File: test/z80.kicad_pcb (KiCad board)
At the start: 2 copper layers, 71.1 x 43.2 mm, 53 parts, among them U1 74AHC1G14

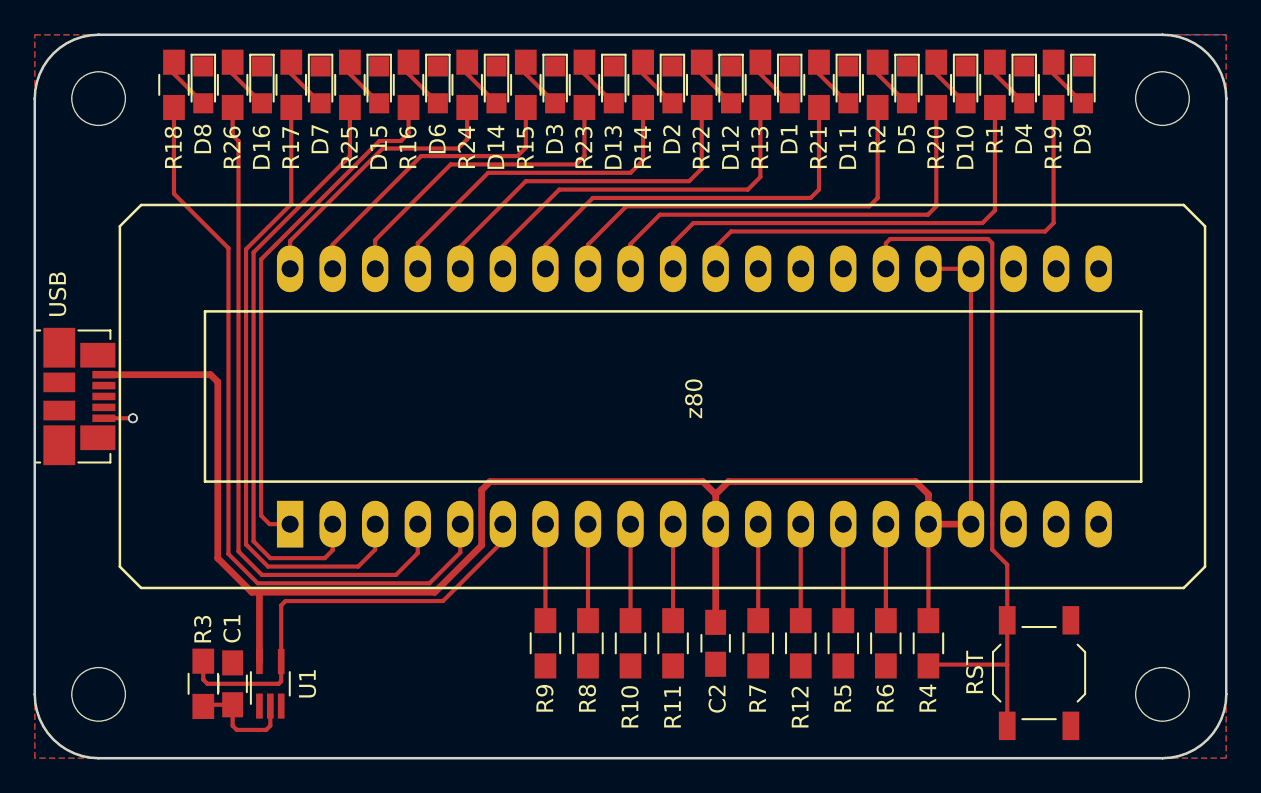
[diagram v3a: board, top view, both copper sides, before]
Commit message: Renumber data pulldowns and address LEDs to match bits
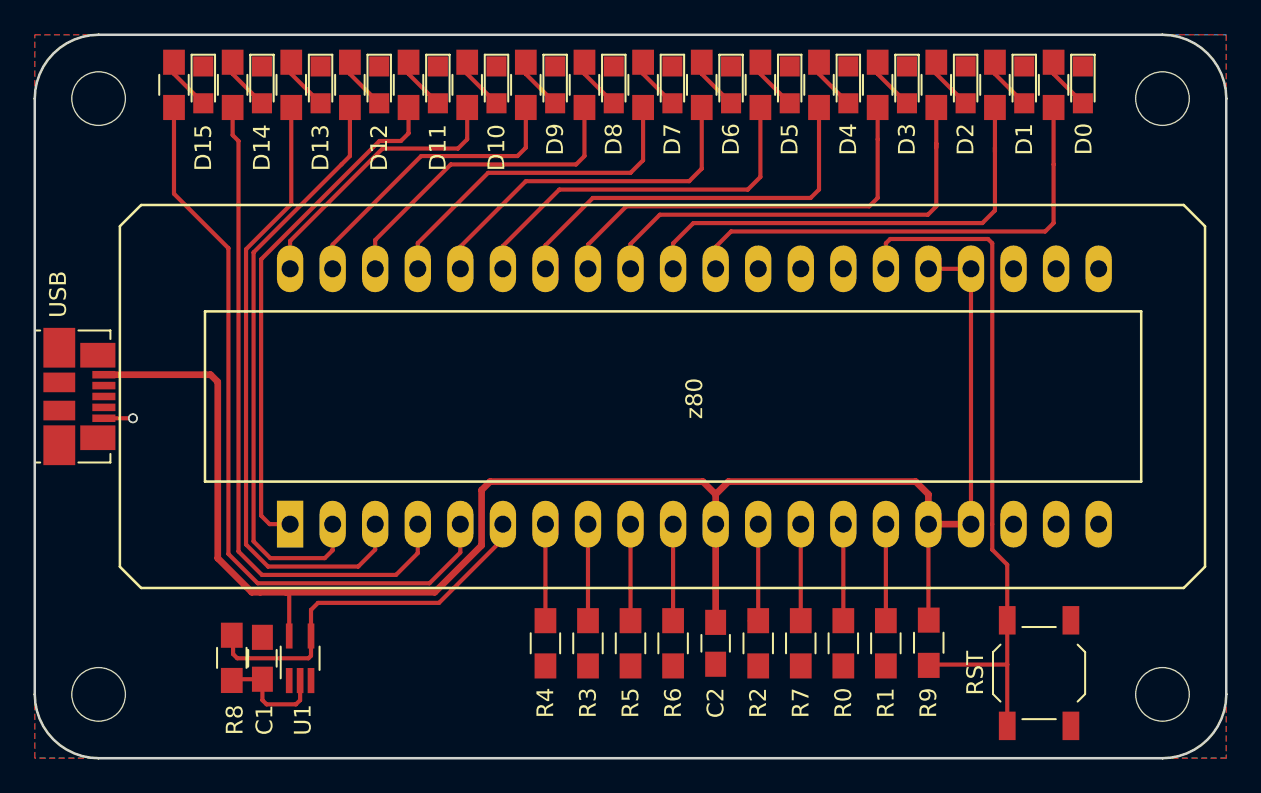
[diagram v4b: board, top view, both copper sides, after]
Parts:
- removed D16: LED, LEDs:LED_0805
- removed R12: 10k, Resistors_SMD:R_0805_HandSoldering
- added D0: LED, LEDs:LED_0805, F.Cu at (217.5, 83.0)
- added R0: 10k, Resistors_SMD:R_0805_HandSoldering, F.Cu at (203.2, 116.3)
- R1, R2: value 470R -> 10k
- R10, R11: value 10k -> 470R
- R3: value 68k -> 10k
- R8: value 10k -> 68k
- moved R10 39.8 mm to (212.2, 83.0), turned to 270 degrees
- moved R11 35.5 mm to (205.2, 83.0), turned to 270 degrees
- moved R2 34.1 mm to (198.1, 116.3), turned to 90 degrees
- moved R1 34.0 mm to (205.7, 116.3), turned to 90 degrees
- moved D9 31.5 mm to (186.0, 83.0)
- moved D10 28.0 mm to (182.5, 83.0)
- moved D11 24.5 mm to (179.0, 83.0)
- moved D8 24.5 mm to (189.5, 83.0)
- moved R3 23.1 mm to (188.0, 116.3), turned to 90 degrees
- moved R9 22.9 mm to (208.3, 116.3), turned to 270 degrees
- moved R4 22.9 mm to (185.4, 116.3), turned to 90 degrees
- moved R8 21.3 mm to (166.7, 117.2), turned to 270 degrees
- moved D12 21.0 mm to (175.5, 83.0)
- moved D3 21.0 mm to (207.0, 83.0)
- moved D7 21.0 mm to (193.0, 83.0)
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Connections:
- R1 pad 1: Net-(D4-Pad2) -> GND
- R10 pad 1: GND -> Net-(D1-Pad2)
- R11 pad 1: GND -> Net-(D3-Pad2)
- R13 pad 1: Net-(D1-Pad2) -> Net-(D5-Pad2)
- R14 pad 1: Net-(D2-Pad2) -> Net-(D7-Pad2)
- R15 pad 1: Net-(D3-Pad2) -> Net-(D9-Pad2)
- R16 pad 1: Net-(D6-Pad2) -> Net-(D11-Pad2)
- R17 pad 1: Net-(D7-Pad2) -> Net-(D13-Pad2)
- R18 pad 1: Net-(D8-Pad2) -> Net-(D15-Pad2)
- R19 pad 1: Net-(D9-Pad2) -> Net-(D0-Pad2)
- R2 pad 1: Net-(D5-Pad2) -> GND
- R20 pad 1: Net-(D10-Pad2) -> Net-(D2-Pad2)
- R21 pad 1: Net-(D11-Pad2) -> Net-(D4-Pad2)
- R22 pad 1: Net-(D12-Pad2) -> Net-(D6-Pad2)
- R23 pad 1: Net-(D13-Pad2) -> Net-(D8-Pad2)
- R24 pad 1: Net-(D14-Pad2) -> Net-(D10-Pad2)
- R25 pad 1: Net-(D15-Pad2) -> Net-(D12-Pad2)
- R26 pad 1: Net-(D16-Pad2) -> Net-(D14-Pad2)
- R3 pad 1: Net-(R3-Pad1) -> GND
- R3 pad 2: Net-(C1-Pad1) -> Net-(R3-Pad2)
- R4 pad 1: VCC -> GND
- R8 pad 1: GND -> Net-(R8-Pad1)
- R8 pad 2: Net-(R8-Pad2) -> Net-(C1-Pad1)
- R9 pad 1: GND -> VCC
- RST1 pad 2: Net-(R4-Pad2) -> Net-(R9-Pad2)
- U1 pad 4: Net-(R3-Pad1) -> Net-(R8-Pad1)
- z80 pad 10: Net-(R11-Pad2) -> Net-(R6-Pad2)
- z80 pad 12: Net-(R7-Pad2) -> Net-(R2-Pad2)
- z80 pad 13: Net-(R12-Pad2) -> Net-(R7-Pad2)
- z80 pad 14: Net-(R5-Pad2) -> Net-(R0-Pad2)
- z80 pad 15: Net-(R6-Pad2) -> Net-(R1-Pad2)
- z80 pad 26: Net-(R4-Pad2) -> Net-(R9-Pad2)
- z80 pad 31: Net-(R1-Pad2) -> Net-(R10-Pad2)
- z80 pad 33: Net-(R2-Pad2) -> Net-(R11-Pad2)
- z80 pad 6: Net-(R3-Pad1) -> Net-(R8-Pad1)
- z80 pad 7: Net-(R9-Pad2) -> Net-(R4-Pad2)
- z80 pad 8: Net-(R8-Pad2) -> Net-(R3-Pad2)
- z80 pad 9: Net-(R10-Pad2) -> Net-(R5-Pad2)
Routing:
- net Net-(R4-Pad2): track 42.0 -> 8.05 mm
- net Net-(R9-Pad2): track 8.05 -> 42.0 mm
- net Net-(R3-Pad1): track 27.3 -> 0.00 mm
- net Net-(R8-Pad1): track 0.00 -> 24.8 mm
- net Net-(R1-Pad2): track 27.9 -> 5.76 mm
- net Net-(R10-Pad2): track 6.52 -> 27.9 mm
- net Net-(R11-Pad2): track 5.76 -> 25.3 mm
- net Net-(R2-Pad2): track 25.3 -> 6.48 mm
- net Net-(R12-Pad2): track 7.03 -> 0.00 mm
- net Net-(R0-Pad2): track 0.00 -> 6.27 mm
- net Net-(R8-Pad2): track 5.76 -> 0.00 mm
- net Net-(R3-Pad2): track 0.00 -> 5.76 mm
- net Net-(D16-Pad2): track 3.17 -> 0.00 mm
- net Net-(D0-Pad2): track 0.00 -> 3.17 mm
- net VCC: track 107.4 -> 106.0 mm
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
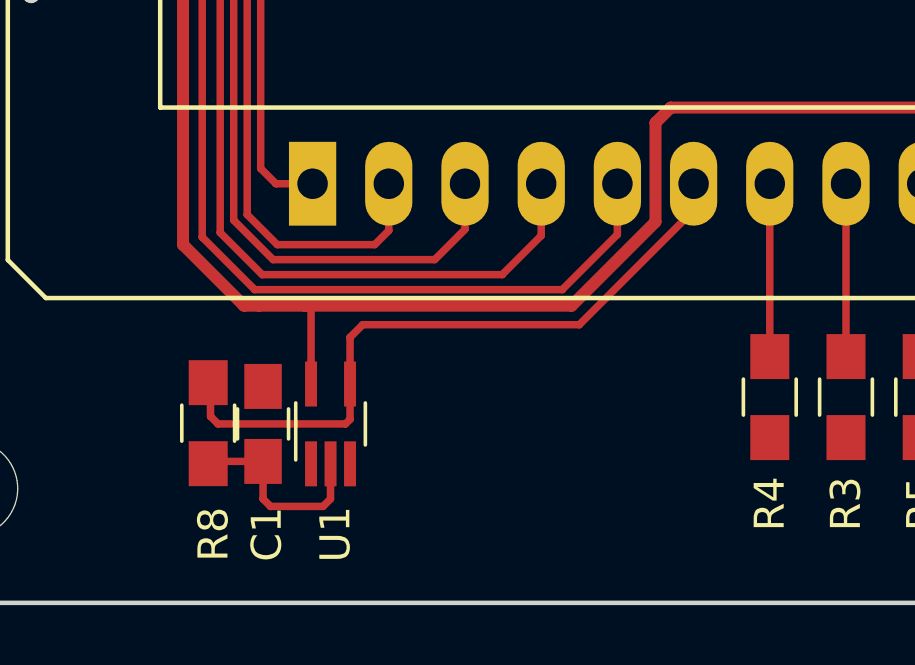
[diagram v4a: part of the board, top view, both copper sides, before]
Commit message: Added jumper on clock signal and replaced C1 with THT footprint.
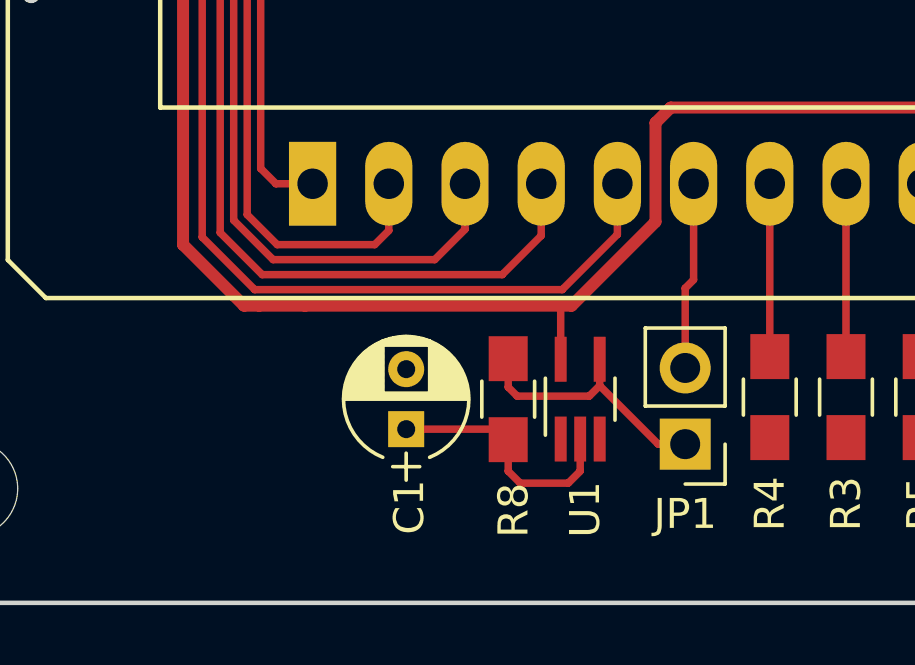
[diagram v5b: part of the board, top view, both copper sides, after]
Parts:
- removed REF***: OSHW-Symbol_6.7x6mm_SilkScreen, Symbols:OSHW-Symbol_6.7x6mm_SilkScreen
- added JP1: Jumper, Pin_Headers:Pin_Header_Straight_1x02_Pitch2.54mm, F.Cu at (182.6, 117.9)
- C1: footprint Capacitors_SMD:C_0805_HandSoldering -> Capacitors_THT:CP_Radial_D4.0mm_P2.00mm
- moved R8 10.0 mm to (176.7, 116.4)
- moved U1 8.36 mm to (179.1, 116.4)
- moved C1 4.78 mm to (173.3, 117.4)
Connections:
- R8 pad 1: Net-(R8-Pad1) -> Net-(JP1-Pad1)
- U1 pad 4: Net-(R8-Pad1) -> Net-(JP1-Pad1)
- z80 pad 6: Net-(R8-Pad1) -> Net-(JP1-Pad2)
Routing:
- net Net-(R8-Pad1): track 24.8 -> 0.00 mm
- net Net-(JP1-Pad2): track 0.00 -> 9.18 mm
- net Net-(JP1-Pad1): track 0.00 -> 8.81 mm
- net Net-(C1-Pad1): track 6.67 -> 8.40 mm
- net VCC: track 106.0 -> 105.1 mm

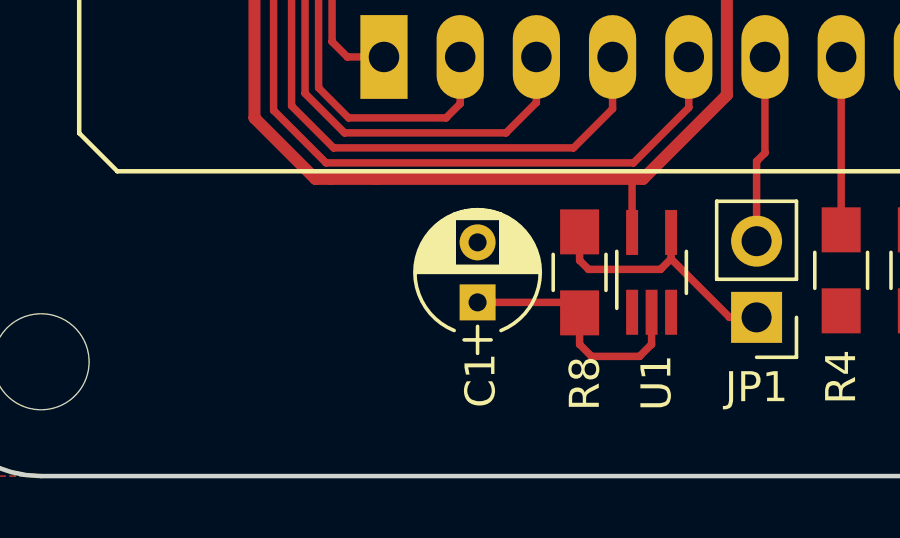
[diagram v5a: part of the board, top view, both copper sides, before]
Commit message: Replaced clock charge cap footprint with ceramic cap
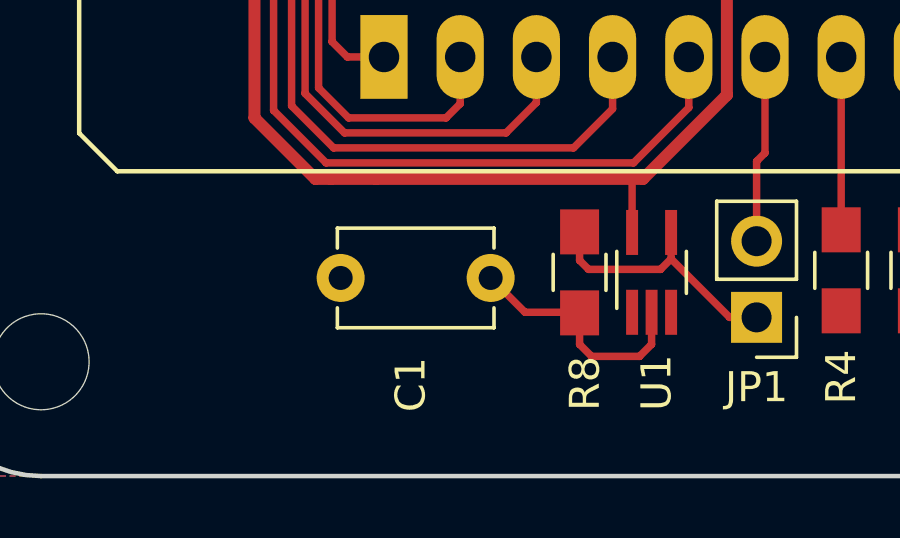
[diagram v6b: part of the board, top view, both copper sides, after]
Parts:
- C1: footprint Capacitors_THT:CP_Radial_D4.0mm_P2.00mm -> Capacitors_THT:C_Disc_D5.1mm_W3.2mm_P5.00mm
- moved C1 0.92 mm to (173.7, 116.6), turned to 180 degrees
